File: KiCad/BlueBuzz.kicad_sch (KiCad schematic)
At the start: 11 parts, among them J1 Conn_01x06_Socket, J2 DE9, SW1 SW_DIP_x01, SW2 SW_DIP_x01, U1 ESP32, U2 AMS1117

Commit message: update PCB
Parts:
- removed J1: Conn_01x06_Socket, Connector_Harwin:Harwin_M20-89006xx_1x06_P2.54mm_Horizontal, symbol Connector:Conn_01x06_Socket
- added J1, J2, J5, J6: Conn_01x01_Socket, Connector_Wire:SolderWirePad_1x01_SMD_1x2mm, symbol Connector:Conn_01x01_Socket
- added J3: Conn_01x03_Socket, Jumper:SolderJumper-3_P1.3mm_Open_Pad1.0x1.5mm_NumberLabels, symbol Connector:Conn_01x03_Socket
- added J4: Conn_01x02_Socket, Jumper:SolderJumper-2_P1.3mm_Open_Pad1.0x1.5mm, symbol Connector:Conn_01x02_Socket
- renumbered J2 to J0
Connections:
- net at U1.35 (TXD0/IO1): now also J1.1 (Pin_1), J3.2 (Pin_2)
- net at U1.34 (RXD0/IO3): now also J2.1 (Pin_1), J3.3 (Pin_3)
- net at C1.2, J0.5, U2.3 (VI): now also J4.2 (Pin_2), J5.1 (Pin_1)
- net at C1.1, C2.1, J0.9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: now also J3.1 (Pin_1), J4.1 (Pin_1), J6.1 (Pin_1)

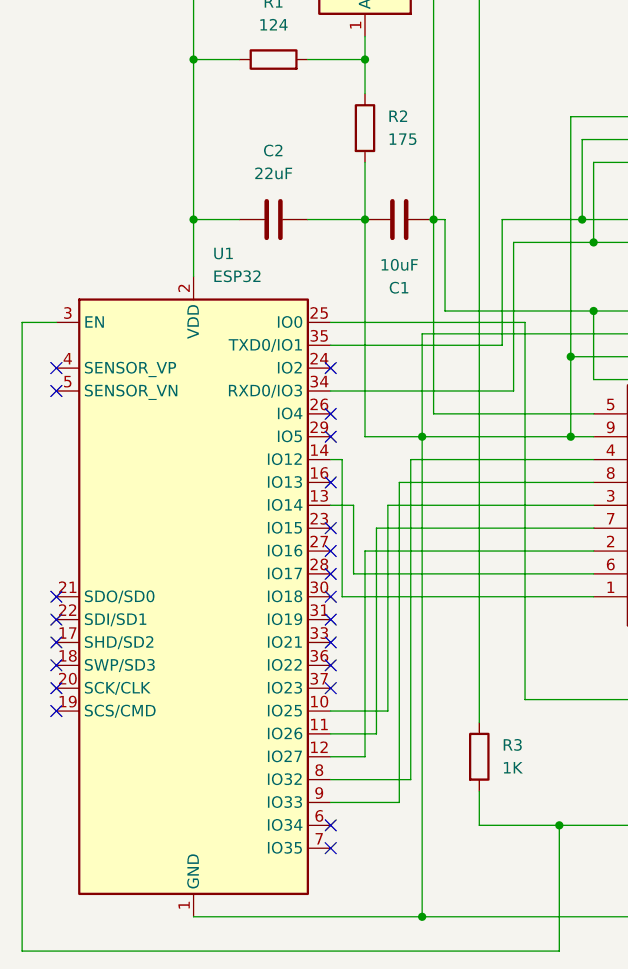
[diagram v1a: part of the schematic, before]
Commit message: 상태표시 LED 추가. 입력 전압 3.3V 변환 로직 추가. 핀배열 변경. 사용법 변경.
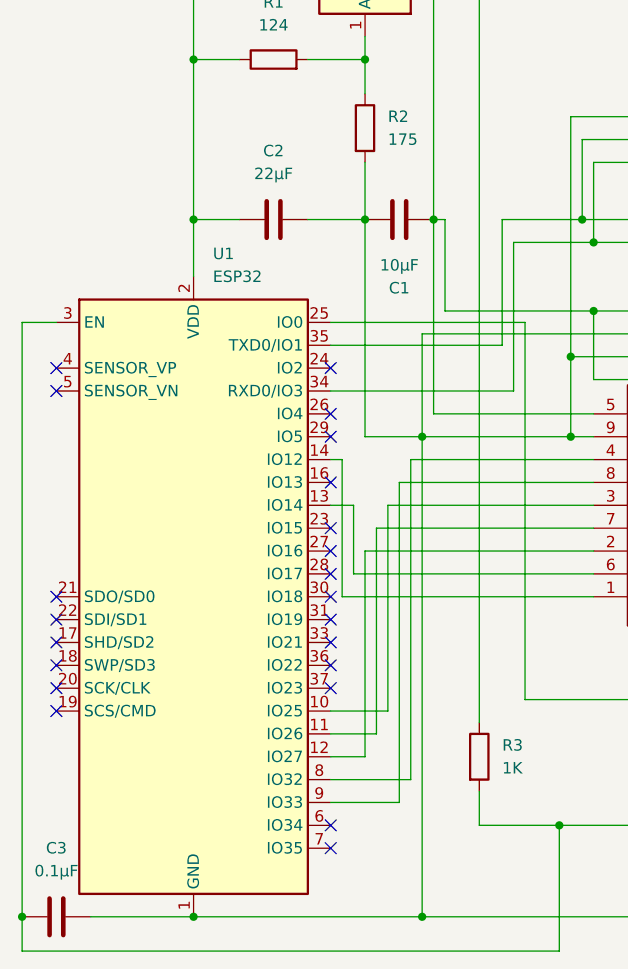
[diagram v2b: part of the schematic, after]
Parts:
- added C3: 0.1μF, Capacitor_SMD:C_0805_2012Metric, symbol Device:C
- C1: value 10uF -> 10μF
- C2: value 22uF -> 22μF
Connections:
- net at C1.1, C2.1, J0.9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: now also C3.2
- net at R3.2, SW2.1, U1.3 (EN): now also C3.1
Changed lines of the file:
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@@
+	)
+	(junction
+		(at 127 134.62)
+		(diameter 0)
+		(color 0 0 0 0)
 	)
 	(junction
@@
 		(color 0 0 0 0)
 	)
+	(junction
+		(at 107.95 134.62)
+		(diameter 0)
+		(color 0 0 0 0)
+	)
 	(no_connect
 		(at 142.24 91.44)
@@
 	(wire
 		(pts
+			(xy 115.57 134.62) (xy 127 134.62)
+		)
+		(stroke
+			(width 0)
+			(type default)
+		)
+	)
+	(wire
+		(pts
 			(xy 154.94 67.31) (xy 171.45 67.31)
 		)
@@
 	(wire
 		(pts
-			(xy 107.95 68.58) (xy 107.95 138.43)
+			(xy 107.95 68.58) (xy 107.95 134.62)
 		)
 		(stroke
@@
 	(wire
 		(pts
+			(xy 107.95 134.62) (xy 107.95 138.43)
+		)
+		(stroke
+			(width 0)
+			(type default)
+		)
+	)
+	(wire
+		(pts
 			(xy 142.24 116.84) (xy 146.05 116.84)
 		)
@@
 			(width 0)
 			(type default)
+		)
+	)
+	(symbol
+		(lib_id "Device:C")
+		(at 111.76 134.62 90)
+		(unit 1)
+		(exclude_from_sim no)
+		(in_bom yes)
+		(on_board yes)
+		(dnp no)
+		(fields_autoplaced yes)
+		(property "Reference" "C3"
+			(at 111.76 127 90)
+			(effects
+				(font
+					(size 1.27 1.27)
+				)
+			)
+		)
+		(property "Value" "0.1μF"
+			(at 111.76 129.54 90)
+			(effects
+				(font
+					(size 1.27 1.27)
+				)
+			)
+		)
+		(property "Footprint" "Capacitor_SMD:C_0805_2012Metric"
+			(at 115.57 133.6548 0)
+			(effects
+				(font
+					(size 1.27 1.27)
+				)
+				(hide yes)
+			)
+		)
+		(property "Datasheet" "~"
+			(at 111.76 134.62 0)
+			(effects
+				(font
+					(size 1.27 1.27)
+				)
+				(hide yes)
+			)
+		)
+		(property "Description" "Unpolarized capacitor"
+			(at 111.76 134.62 0)
+			(effects
+				(font
+					(size 1.27 1.27)
+				)
+				(hide yes)
+			)
+		)
+		(pin "2"
+		)
+		(pin "1"
+		)
+		(instances
+			(project ""
+				(path "/b867b0b1-4ffe-456a-ad13-b7cef3a60a7e"
+					(reference "C3")
+					(unit 1)
+				)
+			)
 		)
 	)
@@
 			)
 		)
-		(property "Value" "22uF"
+		(property "Value" "22μF"
 			(at 135.89 52.07 90)
 			(effects
@@
 			)
 		)
-		(property "Value" "10uF"
+		(property "Value" "10μF"
 			(at 149.86 62.23 90)
 			(effects
